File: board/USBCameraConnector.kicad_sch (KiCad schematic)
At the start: 6 parts, among them J1 USB4105-GF-A, J7 Conn_01x04_Pin

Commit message: Done
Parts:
- J7: footprint Connector_PinHeader_2.54mm:PinHeader_1x04_P2.54mm_Vertical -> Connector_PinHeader_2.00mm:PinHeader_1x04_P2.00mm_Vertical
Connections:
- net DN: now also J7.2 (Pin_2); no longer J7.3 (Pin_3)
- net DP: now also J7.3 (Pin_3); no longer J7.2 (Pin_2)
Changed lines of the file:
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@@
+	(wire
+		(pts
+			(xy 199.39 83.82) (xy 208.28 83.82)
+		)
+		(stroke
+			(width 0)
+			(type default)
+		)
+	)
+	(wire
+		(pts
+			(xy 199.39 81.28) (xy 208.28 81.28)
+		)
+		(stroke
+			(width 0)
+			(type default)
+		)
+	)
 	(wire
 		(pts
@@
 		(pts
 			(xy 147.32 66.04) (xy 157.48 66.04)
-		)
-		(stroke
-			(width 0)
-			(type default)
-		)
-	)
-	(wire
-		(pts
-			(xy 200.66 81.28) (xy 208.28 81.28)
-		)
-		(stroke
-			(width 0)
-			(type default)
-		)
-	)
-	(wire
-		(pts
-			(xy 200.66 83.82) (xy 208.28 83.82)
 		)
 		(stroke
@@
 	(global_label "DN"
 		(shape input)
-		(at 200.66 81.28 180)
+		(at 199.39 83.82 180)
 		(fields_autoplaced yes)
 		(effects
@@
 		)
 		(property "Intersheetrefs" "${INTERSHEET_REFS}"
-			(at 195.0743 81.28 0)
+			(at 193.8043 83.82 0)
 			(effects
 				(font
@@
 	(global_label "DP"
 		(shape input)
-		(at 200.66 83.82 180)
+		(at 199.39 81.28 180)
 		(fields_autoplaced yes)
 		(effects
@@
 		)
 		(property "Intersheetrefs" "${INTERSHEET_REFS}"
-			(at 195.1348 83.82 0)
+			(at 193.8648 81.28 0)
 			(effects
 				(font
@@
 			)
 		)
-		(property "Footprint" "Connector_PinHeader_2.54mm:PinHeader_1x04_P2.54mm_Vertical"
+		(property "Footprint" "Connector_PinHeader_2.00mm:PinHeader_1x04_P2.00mm_Vertical"
 			(at 213.36 83.82 0)
 			(effects

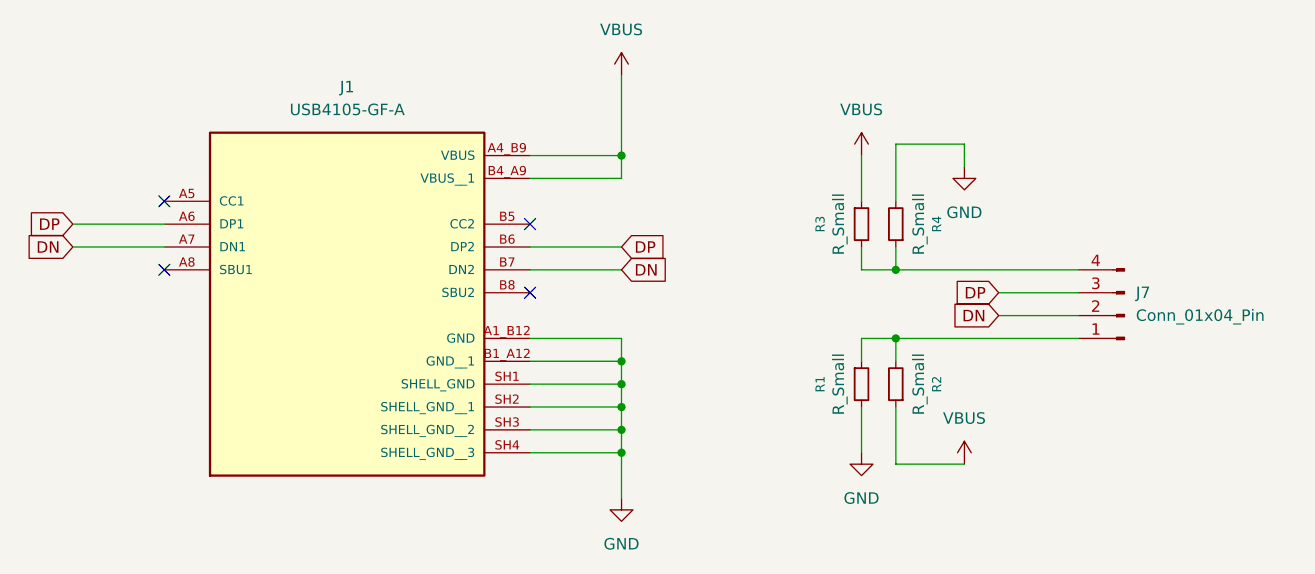
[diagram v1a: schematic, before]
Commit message: Better GND vias
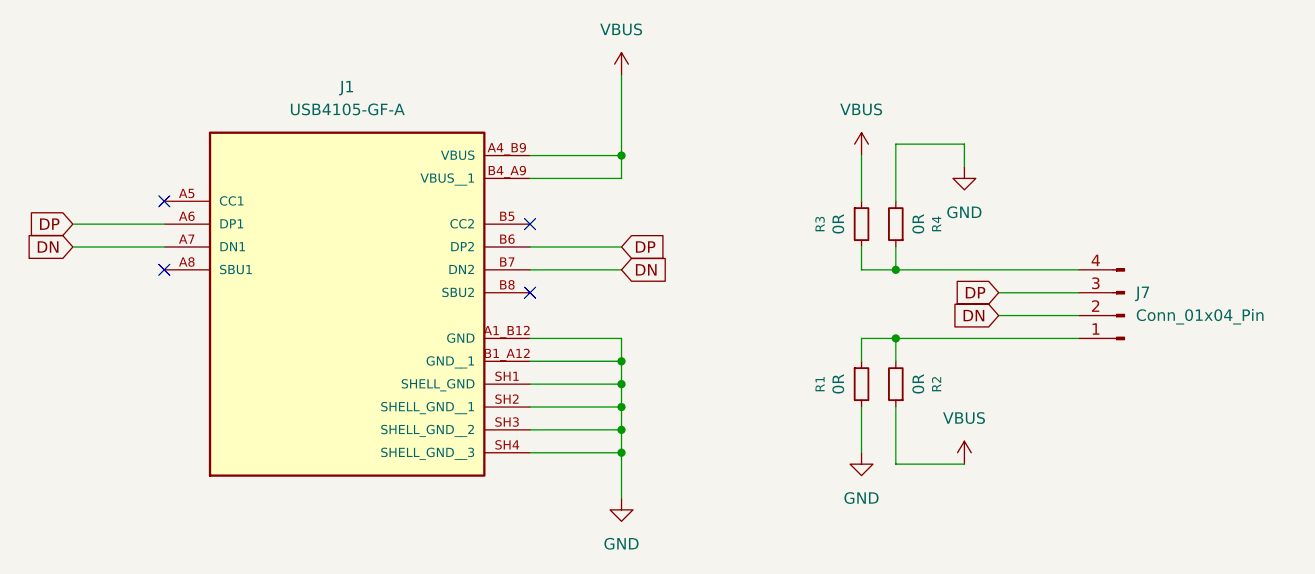
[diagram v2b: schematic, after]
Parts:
- R1, R2, R3, R4: value R_Small -> 0R
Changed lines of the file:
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@@
 			)
 		)
-		(property "Value" "R_Small"
+		(property "Value" "0R"
 			(at 181.61 73.66 90)
 			(effects
@@
 			)
 		)
-		(property "Value" "R_Small"
+		(property "Value" "0R"
 			(at 181.61 91.44 90)
 			(effects
@@
 			)
 		)
-		(property "Value" "R_Small"
+		(property "Value" "0R"
 			(at 190.5 73.66 90)
 			(effects
@@
 			)
 		)
-		(property "Value" "R_Small"
+		(property "Value" "0R"
 			(at 190.5 91.44 90)
 			(effects
